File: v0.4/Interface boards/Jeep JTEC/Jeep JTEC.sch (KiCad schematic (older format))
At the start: 16 parts, among them J1 Conn_02x20_Counter_Clockwise, J2 12v SW Output

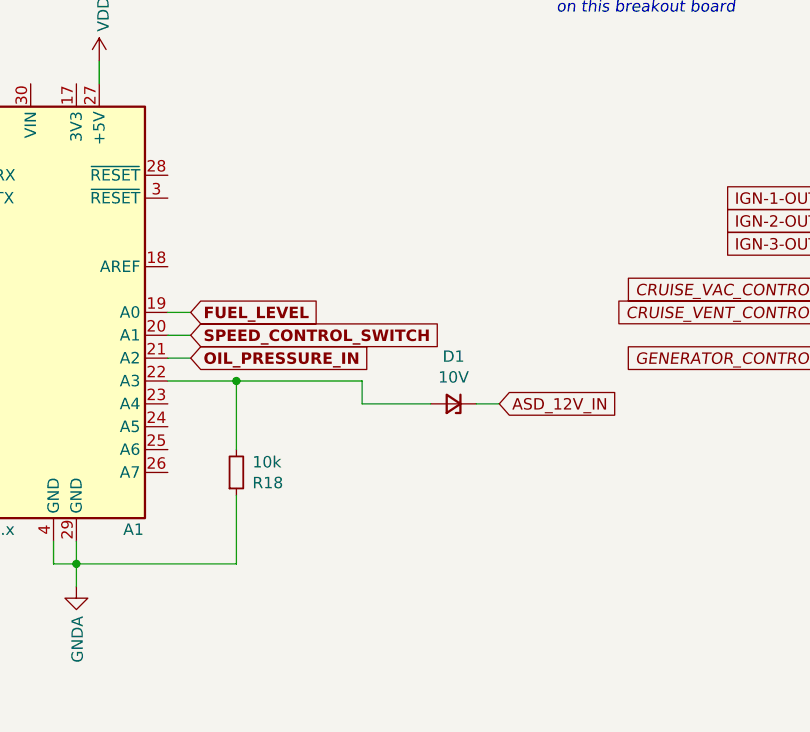
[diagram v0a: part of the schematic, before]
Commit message: Add pull up resistor to cruise control input
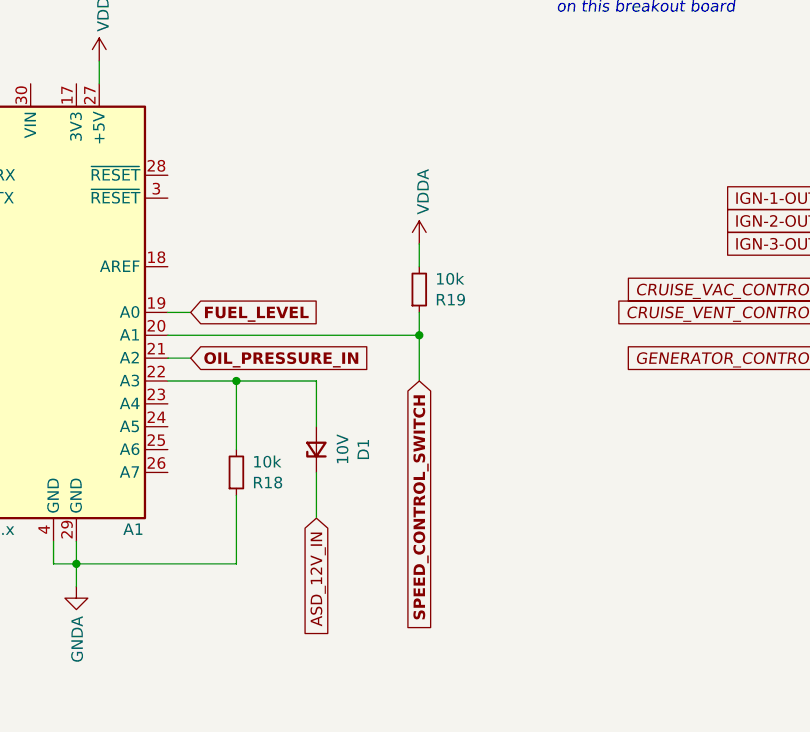
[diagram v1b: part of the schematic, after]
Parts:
- added R19: 10k, Resistor_SMD:R_0805_2012Metric, symbol Device:R_Small
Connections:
- net SPEED_CONTROL_SWITCH: now also R19.1
- net VDDA: now also R19.2
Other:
- moved on the sheet: D1
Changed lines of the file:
@@
 Wire Wire Line
 	5250 7100 5250 7000
-Wire Wire Line
-	5750 6000 5650 6000
 Text GLabel 9250 4100 0    50   Input ~ 10
 SPEED_CONTROL_SWITCH
-Text GLabel 5750 6000 2    50   Input ~ 10
+Text GLabel 6750 6200 3    50   Input ~ 10
 SPEED_CONTROL_SWITCH
 Text GLabel 7050 3200 0    50   Input ~ 10
@@
 L Misc:D_Zener_SOT-23 D1
 U 1 1 618B7D29
-P 6900 6300
-F 0 "D1" H 6900 6093 50  0000 C CNN
-F 1 "10V" H 6900 6184 50  0000 C CNN
-F 2 "Package_TO_SOT_SMD:SOT-23" V 6900 6300 50  0001 C CNN
-F 3 "~" V 6900 6300 50  0001 C CNN
-F 4 "BZX84-C10,215" H 6900 6300 50  0001 C CNN "Manufacturer"
-F 5 "Nexperia USA Inc." H 6900 6300 50  0001 C CNN "Manufacturer#"
-F 6 "1727-2935-1-ND" H 6900 6300 50  0001 C CNN "digikey#"
-	1    6900 6300
-	-1   0    0    1
-$EndComp
-Wire Wire Line
-	7000 6300 7100 6300
-Wire Wire Line
-	6500 6200 6500 6300
-Wire Wire Line
-	6500 6300 6800 6300
-Wire Wire Line
-	5950 6200 6500 6200
-Text GLabel 7100 6300 2    50   Input ~ 0
+P 6300 6500
+F 0 "D1" H 6300 6293 50  0000 C CNN
+F 1 "10V" H 6300 6384 50  0000 C CNN
+F 2 "Package_TO_SOT_SMD:SOT-23" V 6300 6500 50  0001 C CNN
+F 3 "~" V 6300 6500 50  0001 C CNN
+F 4 "BZX84-C10,215" H 6300 6500 50  0001 C CNN "Manufacturer"
+F 5 "Nexperia USA Inc." H 6300 6500 50  0001 C CNN "Manufacturer#"
+F 6 "1727-2935-1-ND" H 6300 6500 50  0001 C CNN "digikey#"
+	1    6300 6500
+	0    -1   -1   0
+$EndComp
+Text GLabel 6300 6800 3    50   Input ~ 0
 ASD_12V_IN
 $Comp
@@
 	1    0    0    -1
 $EndComp
+Wire Wire Line
+	5950 6200 6300 6200
+Wire Wire Line
+	6300 6800 6300 6600
+Wire Wire Line
+	6300 6400 6300 6200
+Wire Wire Line
+	6750 6200 6750 6000
+Wire Wire Line
+	5650 6000 6750 6000
+$Comp
+L Device:R_Small R?
+U 1 1 6164377D
+P 6750 5800
+AR Path="/615FCF77/6164377D" Ref="R?"  Part="1"
+AR Path="/6164377D" Ref="R19"  Part="1"
+F 0 "R19" H 6820 5846 50  0000 L CNN
+F 1 "10k" H 6820 5755 50  0000 L CNN
+F 2 "Resistor_SMD:R_0805_2012Metric" V 6680 5800 50  0001 C CNN
+F 3 "~" H 6750 5800 50  0001 C CNN
+F 4 "Yageo" H 6750 5800 50  0001 C CNN "Manufacturer"
+F 5 "RC0805FR-0710KL" H 6750 5800 50  0001 C CNN "Manufacturer#"
+	1    6750 5800
+	1    0    0    1
+$EndComp
+Wire Wire Line
+	6750 6000 6750 5900
+Wire Wire Line
+	6750 5700 6750 5600
+Connection ~ 6750 6000
+$Comp
+L power:VDDA #PWR0104
+U 1 1 6164E774
+P 6750 5600
+F 0 "#PWR0104" H 6750 5450 50  0001 C CNN
+F 1 "VDDA" V 6768 5728 50  0000 L CNN
+F 2 "" H 6750 5600 50  0001 C CNN
+F 3 "" H 6750 5600 50  0001 C CNN
+	1    6750 5600
+	1    0    0    -1
+$EndComp

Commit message: Add BOM and gerbers
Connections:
- net CLT_Sensor: now also A1.23 (A4)
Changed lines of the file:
@@
 	1    0    0    -1
 $EndComp
+Text GLabel 5750 6300 2    50   Input ~ 0
+CLT_Sensor
+Wire Wire Line
+	5750 6300 5650 6300
 $EndSCHEMATC

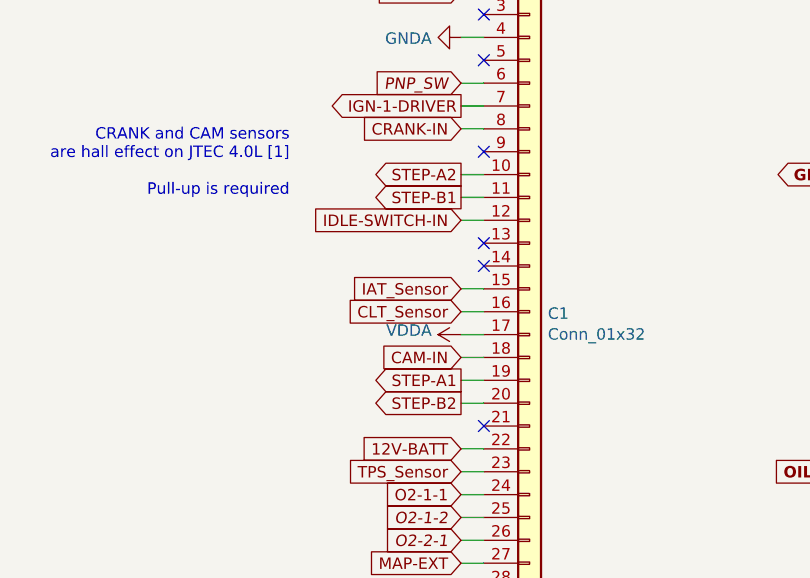
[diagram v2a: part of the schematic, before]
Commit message: Correct stepper IAC phases
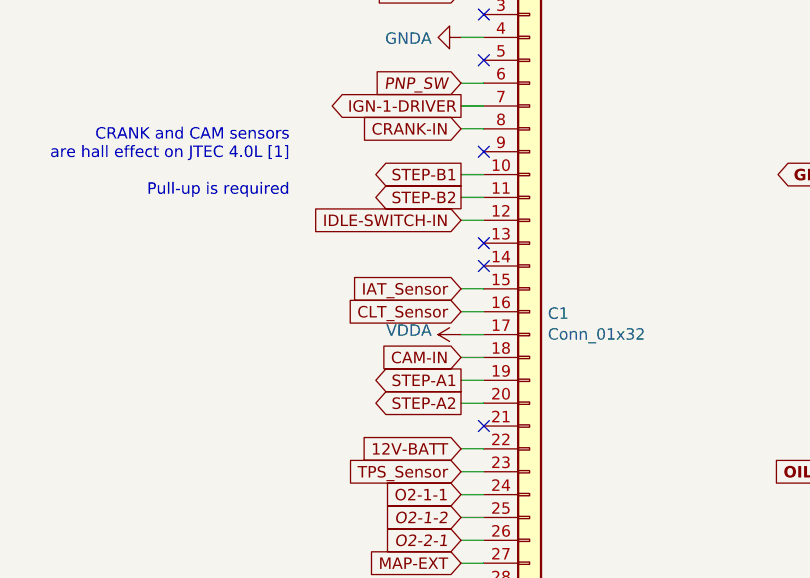
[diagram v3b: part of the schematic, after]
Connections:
- net STEP-A2: now also C1.20 (Pin_20); no longer C1.10 (Pin_10)
- net STEP-B1: now also C1.10 (Pin_10); no longer C1.11 (Pin_11)
- net STEP-B2: now also C1.11 (Pin_11); no longer C1.20 (Pin_20)
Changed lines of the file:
@@
 Text GLabel 4900 2800 0    50   Output ~ 0
 STEP-A1
-Text GLabel 4900 1900 0    50   Output ~ 0
+Text GLabel 4900 2900 0    50   Output ~ 0
 STEP-A2
 Wire Wire Line
@@
 Wire Wire Line
 	4900 1900 5000 1900
-Text GLabel 4900 2000 0    50   Output ~ 0
+Text GLabel 4900 1900 0    50   Output ~ 0
 STEP-B1
 Wire Wire Line
 	4900 2000 5000 2000
-Text GLabel 4900 2900 0    50   Output ~ 0
+Text GLabel 4900 2000 0    50   Output ~ 0
 STEP-B2
 Wire Wire Line

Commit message: Add diodes to igniter circuit to allow ringing
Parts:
- A1: symbol MCU_Module:Arduino_Nano_v3.x -> Shields:Arduino_Nano_v3.x
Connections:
- no-connect marks 37 -> 64
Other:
- note added: "Pressure switch grounded when on and ok"
- note removed: "Pressure switch grounded when ok"
- moved on the sheet: C3, D1, R18

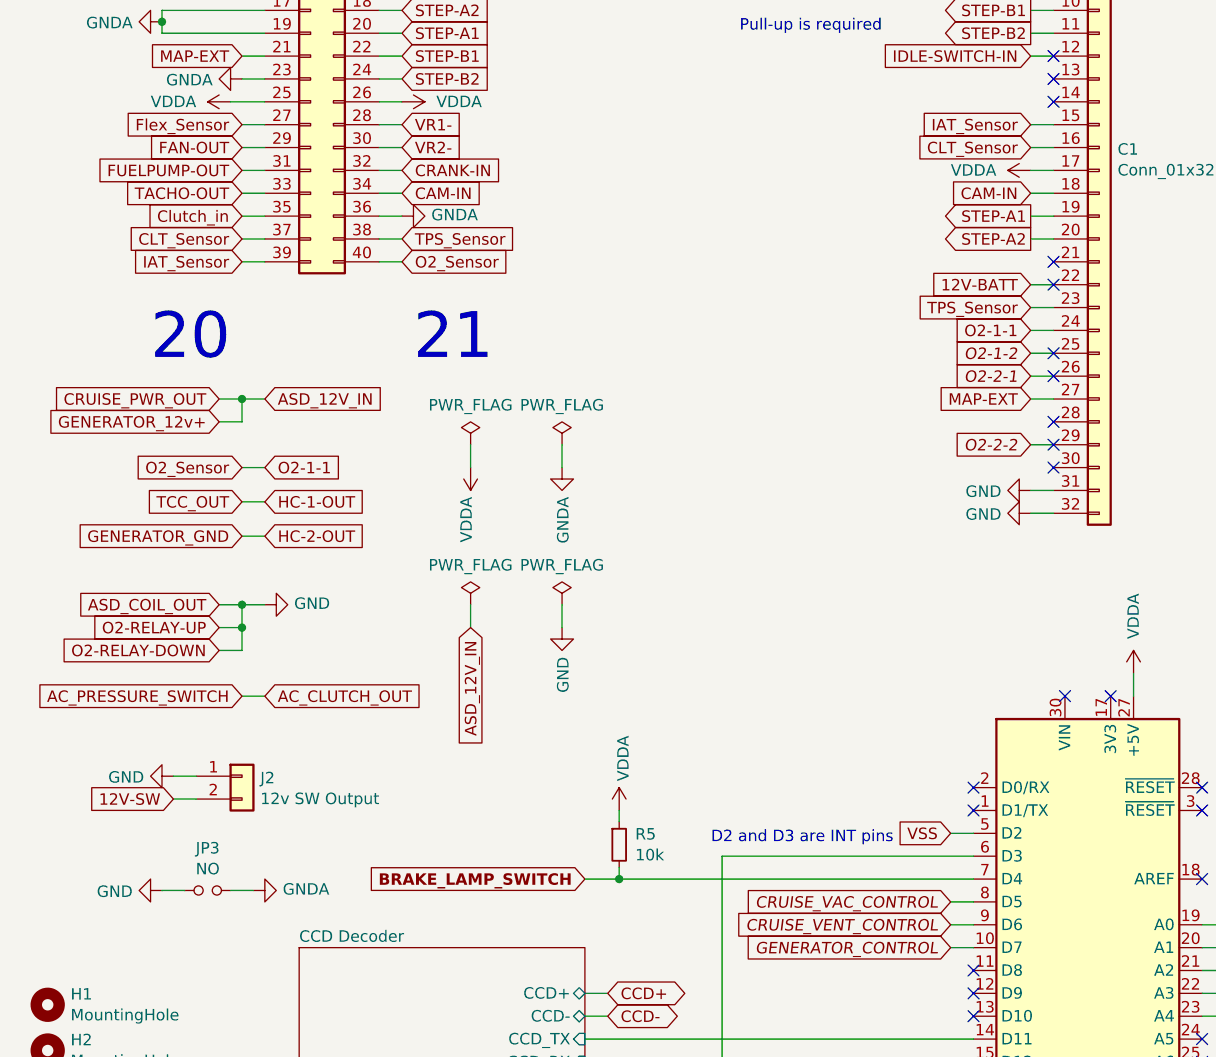
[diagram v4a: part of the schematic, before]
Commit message: Correct drill size for JTEC connector
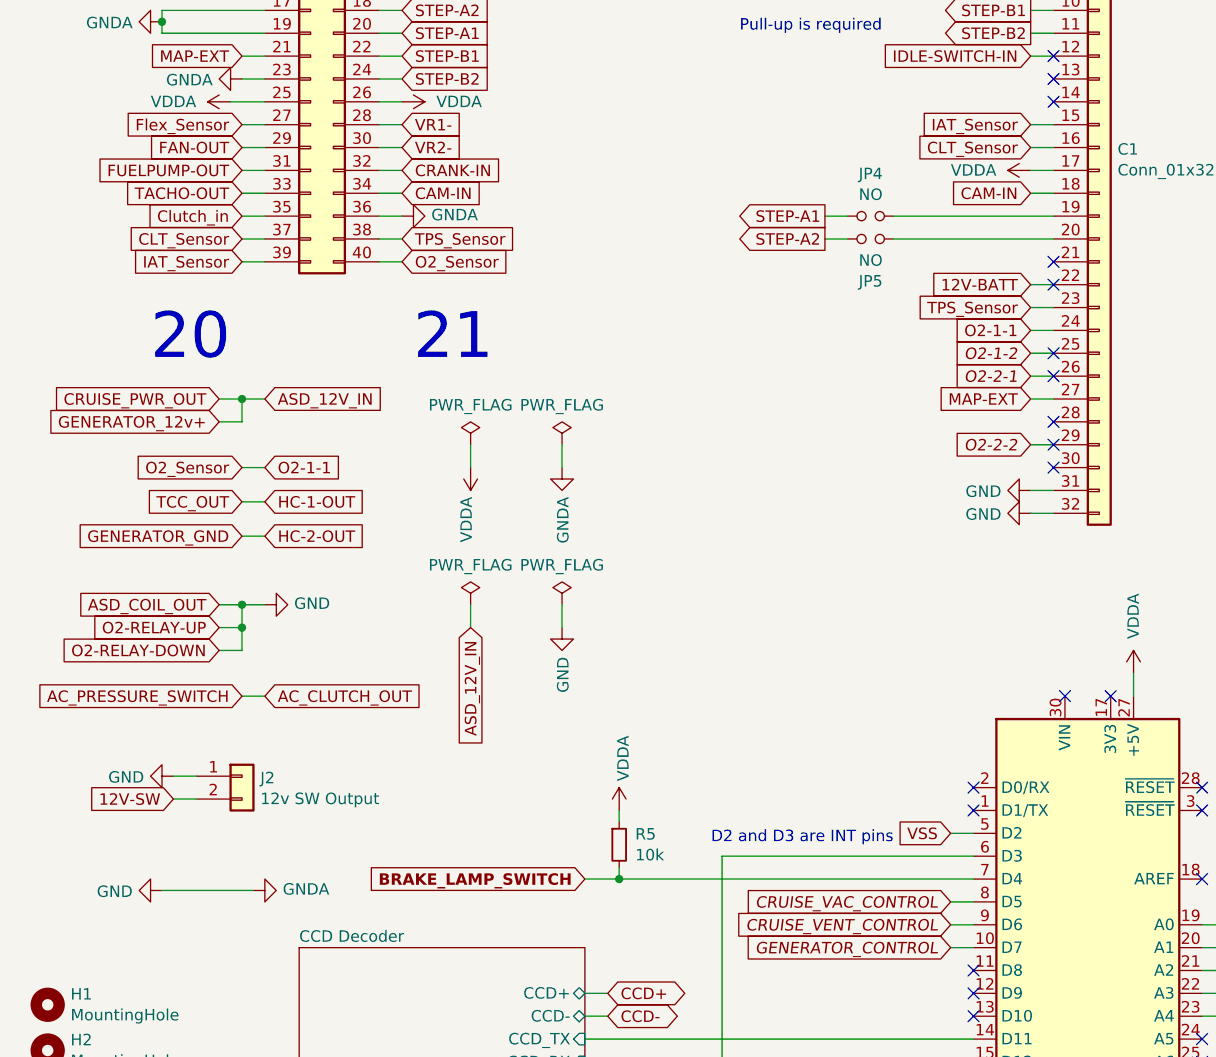
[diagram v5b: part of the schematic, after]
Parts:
- removed JP3: NO, Connector_PinHeader_2.54mm:PinHeader_1x02_P2.54mm_Vertical, symbol Device:Jumper_NO_Small
- added JP4, JP5: NO, Connector_PinHeader_2.54mm:PinHeader_1x02_P2.54mm_Vertical, symbol Device:Jumper_NO_Small
- D1: Manufacturer BZX84-C10,215 -> Nexperia USA Inc.; Manufacturer# Nexperia USA Inc. -> BZX84-C10,215
- J1: Manufacturer 302-S401 -> On Shore Technology Inc.; Manufacturer# On Shore Technology Inc. -> 302-S401
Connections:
- net GNDA is gone; now on net GND: A1.29 (GND), A1.4 (GND), C1.4 (Pin_4), J1.17 (Pin_17), J1.19 (Pin_19), J1.23 (Pin_23), J1.36 (Pin_36), R18.1
- net STEP-A1: now also JP4.1; no longer C1.19 (Pin_19)
- net STEP-A2: now also JP5.2; no longer C1.20 (Pin_20)
- new net: C1.19 (Pin_19), JP4.2
- new net: C1.20 (Pin_20), JP5.1
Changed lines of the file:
@@
 F 2 "Connector_IDC:IDC-Header_2x20_P2.54mm_Vertical" H 1750 2000 50  0001 C CNN
 F 3 "~" H 1750 2000 50  0001 C CNN
-F 4 "302-S401" H 1750 2000 50  0001 C CNN "Manufacturer"
-F 5 "	On Shore Technology Inc." H 1750 2000 50  0001 C CNN "Manufacturer#"
+F 4 "On Shore Technology Inc." H 1750 2000 50  0001 C CNN "Manufacturer"
+F 5 "302-S401	" H 1750 2000 50  0001 C CNN "Manufacturer#"
 F 6 "ED10529-ND" H 1750 2000 50  0001 C CNN "digikey#"
 	1    1750 2000
@@
 Text GLabel 1550 4050 2    50   Input ~ 0
 HC-1-OUT
-Text GLabel 4900 2800 0    50   Output ~ 0
+Text GLabel 4000 2800 0    50   Output ~ 0
 STEP-A1
-Text GLabel 4900 2900 0    50   Output ~ 0
+Text GLabel 4000 2900 0    50   Output ~ 0
 STEP-A2
-Wire Wire Line
-	5000 2800 4900 2800
 Wire Wire Line
 	4900 1900 5000 1900
@@
 Text GLabel 4900 2000 0    50   Output ~ 0
 STEP-B2
-Wire Wire Line
-	5000 2900 4900 2900
 Text Notes 4800 800  0    200  ~ 0
 Black
@@
 F 2 "Package_TO_SOT_SMD:SOT-23" V 6400 6500 50  0001 C CNN
 F 3 "~" V 6400 6500 50  0001 C CNN
-F 4 "BZX84-C10,215" H 6400 6500 50  0001 C CNN "Manufacturer"
-F 5 "Nexperia USA Inc." H 6400 6500 50  0001 C CNN "Manufacturer#"
+F 4 "Nexperia USA Inc." H 6400 6500 50  0001 C CNN "Manufacturer"
+F 5 "BZX84-C10,215" H 6400 6500 50  0001 C CNN "Manufacturer#"
 F 6 "1727-2935-1-ND" H 6400 6500 50  0001 C CNN "digikey#"
 	1    6400 6500
@@
 Text GLabel 1150 5350 0    50   Input ~ 0
 12V-SW
-$Comp
-L Device:Jumper_NO_Small JP3
-U 1 1 61A8768C
-P 1300 5750
-F 0 "JP3" H 1300 5935 50  0000 C CNN
-F 1 "NO" H 1300 5844 50  0000 C CNN
-F 2 "Connector_PinHeader_2.54mm:PinHeader_1x02_P2.54mm_Vertical" H 1300 5750 50  0001 C CNN
-F 3 "~" H 1300 5750 50  0001 C CNN
-F 4 "10129378-902001BLF" H 1300 5750 50  0001 C CNN "Manufacturer"
-F 5 "Amphenol ICC (FCI)" H 1300 5750 50  0001 C CNN "Manufacturer#"
-F 6 "10129378-902001BLF-ND" H 1300 5750 50  0001 C CNN "digikey#"
-	1    1300 5750
-	1    0    0    -1
-$EndComp
-Wire Wire Line
-	1100 5750 1200 5750
-Wire Wire Line
-	1400 5750 1500 5750
 $Comp
 L power:GND #PWR0102
@@
 NoConn ~ 5650 6400
 NoConn ~ 9250 3200
+$Comp
+L Device:Jumper_NO_Small JP4
+U 1 1 61645A04
+P 4200 2800
+F 0 "JP4" H 4200 2985 50  0000 C CNN
+F 1 "NO" H 4200 2894 50  0000 C CNN
+F 2 "Connector_PinHeader_2.54mm:PinHeader_1x02_P2.54mm_Vertical" H 4200 2800 50  0001 C CNN
+F 3 "~" H 4200 2800 50  0001 C CNN
+F 4 "Amphenol ICC (FCI)" H 4200 2800 50  0001 C CNN "Manufacturer"
+F 5 "10129378-902001BLF" H 4200 2800 50  0001 C CNN "Manufacturer#"
+F 6 "10129378-902001BLF-ND" H 4200 2800 50  0001 C CNN "digikey#"
+	1    4200 2800
+	1    0    0    -1
+$EndComp
+$Comp
+L Device:Jumper_NO_Small JP5
+U 1 1 616469B9
+P 4200 2900
+F 0 "JP5" H 4200 3085 50  0000 C CNN
+F 1 "NO" H 4200 2994 50  0000 C CNN
+F 2 "Connector_PinHeader_2.54mm:PinHeader_1x02_P2.54mm_Vertical" H 4200 2900 50  0001 C CNN
+F 3 "~" H 4200 2900 50  0001 C CNN
+F 4 "Amphenol ICC (FCI)" H 4200 2900 50  0001 C CNN "Manufacturer"
+F 5 "10129378-902001BLF" H 4200 2900 50  0001 C CNN "Manufacturer#"
+F 6 "10129378-902001BLF-ND" H 4200 2900 50  0001 C CNN "digikey#"
+	1    4200 2900
+	-1   0    0    1
+$EndComp
+Wire Wire Line
+	4000 2800 4100 2800
+Wire Wire Line
+	4300 2800 5000 2800
+Wire Wire Line
+	4000 2900 4100 2900
+Wire Wire Line
+	4300 2900 5000 2900
+Wire Wire Line
+	1100 5750 1500 5750
 $EndSCHEMATC
